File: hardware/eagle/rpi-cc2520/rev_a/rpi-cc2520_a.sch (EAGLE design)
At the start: 28 parts, among them P1 MOLEX_73251-135X, U1 CC2520, X1 NX2520SA

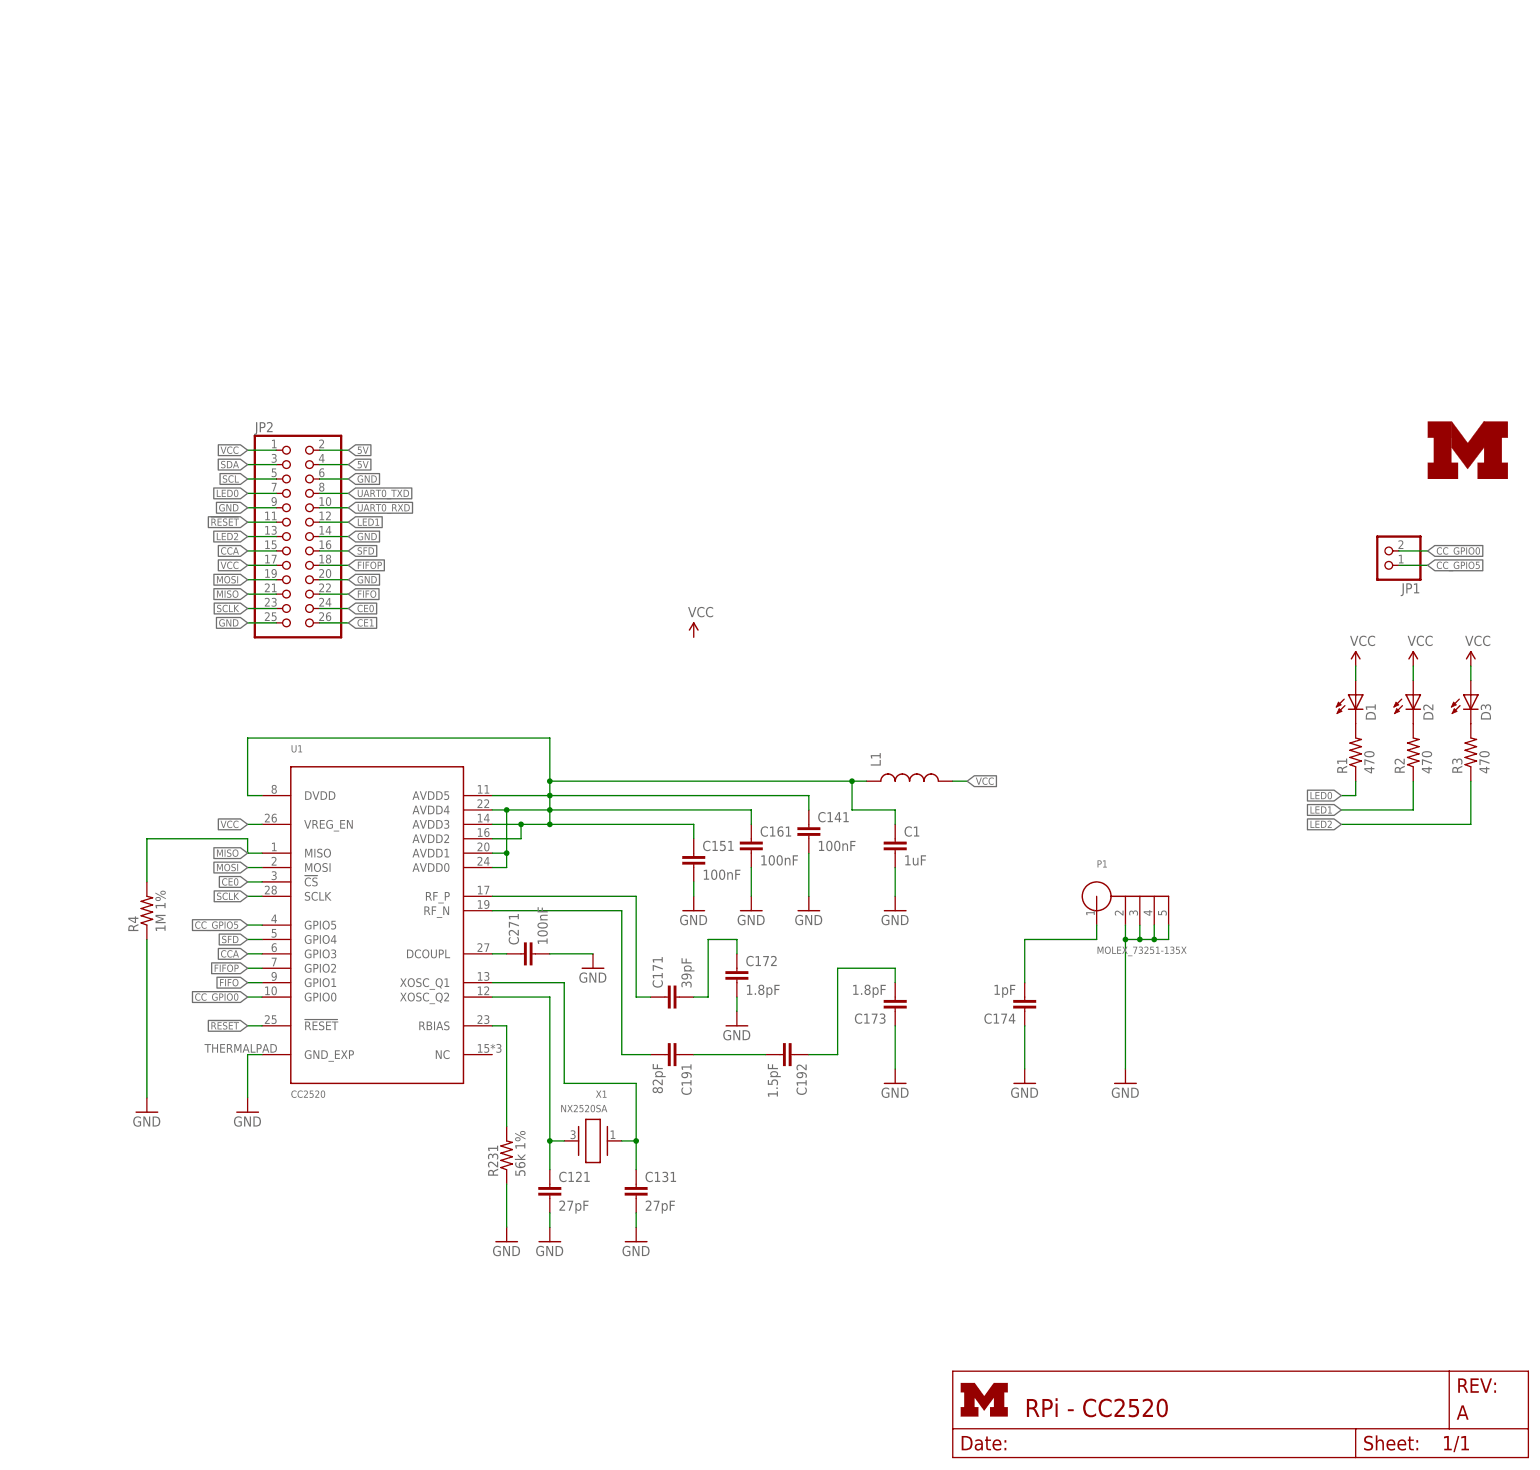
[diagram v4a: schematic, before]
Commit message: carefully laying out the sma antenna
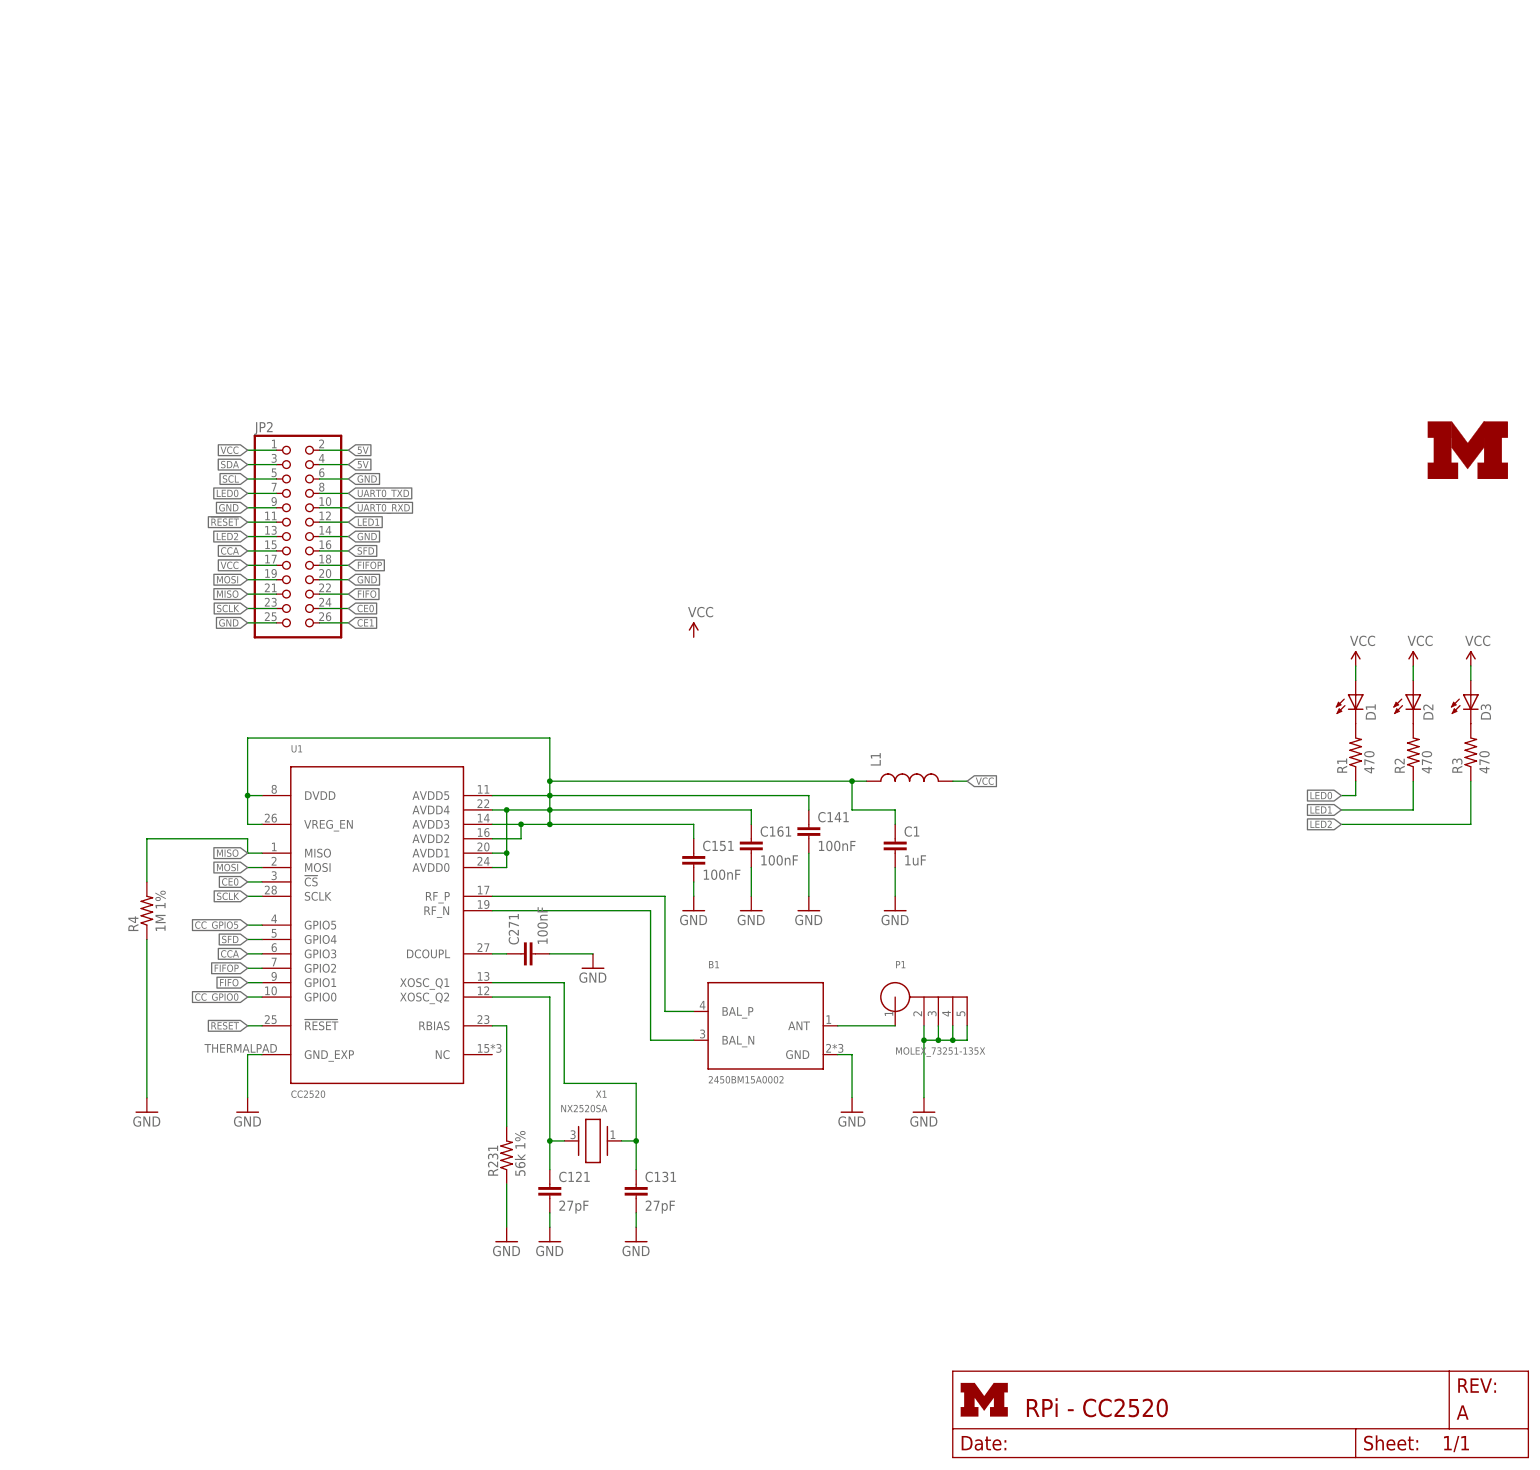
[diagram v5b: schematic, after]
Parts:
- removed C171: 39pF, rcl:C-EUC0402
- removed C172, C173: 1.8pF, rcl:C-EUC0402
- removed C174: 1pF, rcl:C-EUC0402
- removed C191: 82pF, rcl:C-EUC0402
- removed C192: 1.5pF, rcl:C-EUC0402
- removed JP1: (no value), pinhead:PINHD-1X2
- added B1: 2450BM15A0002, rpi-cc2520:2450BM15A0002
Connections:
- removed net N$10: C174.2, P1.P$1
- removed net N$4: C171.1, U1.RF_P
- removed net N$6: C191.2, U1.RF_N
- removed net N$8: C191.1, C192.2
- removed net N$9: C173.2, C192.1
- new net RF_N: B1.BAL_N, U1.RF_N
- new net RF_P: B1.BAL_P, U1.RF_P
- net CC_GPIO0: no longer JP1.2
- net CC_GPIO5: no longer JP1.1
- net GND: now also B1.GND; no longer C172.2, C173.1, C174.1
- net N$5: now also U1.VREG_EN
- net N$7: now also B1.ANT, P1.P$1; no longer C171.2, C172.1
- net VCC: no longer U1.VREG_EN
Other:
- moved on the sheet: P1

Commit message: added a ton of vias
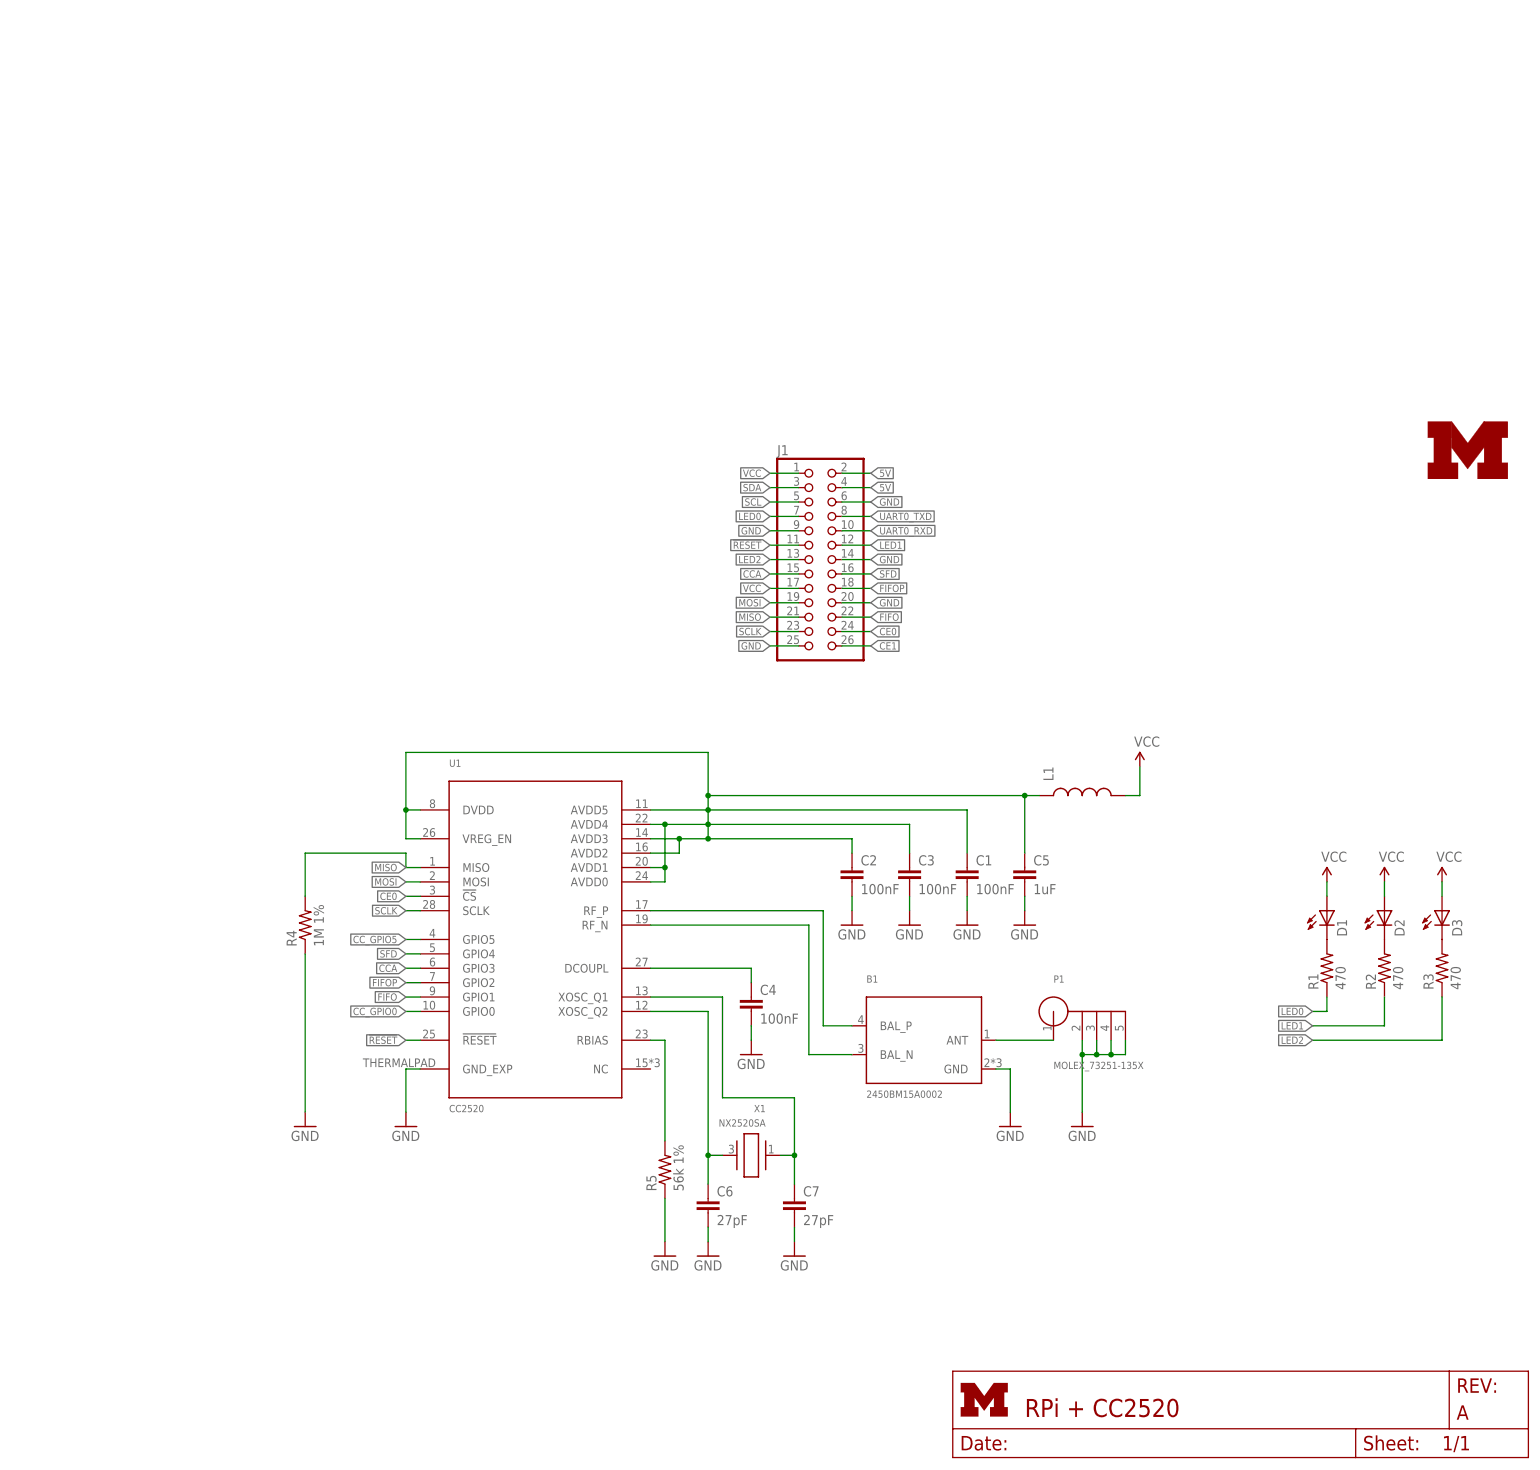
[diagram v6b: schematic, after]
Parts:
- removed C121, C131: 27pF, rcl:C-EUC0402
- removed C141, C151, C161, C271: 100nF, rcl:C-EUC0402
- removed JP2: (no value), pinhead:PINHD-2X13
- removed R231: 56k 1%, rcl:R-US_R0402
- added C2, C3, C4: 100nF, rcl:C-EUC0402
- added C5: 1uF, rcl:C-EUC0603
- added C6, C7: 27pF, rcl:C-EUC0402
- added J1: (no value), pinhead:PINHD-2X13
- added R5: 56k 1%, rcl:R-US_R0402
- C1: value 1uF -> 100nF; device rcl:C-EUC0603 -> rcl:C-EUC0402; DIGIKEY 490-1550-1-ND -> 490-1318-1-ND
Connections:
- net !RESET: now also J1.11; no longer JP2.11
- net 5V: now also J1.2, J1.4; no longer JP2.2, JP2.4
- net CCA: now also J1.15; no longer JP2.15
- net CE0: now also J1.24; no longer JP2.24
- net CE1: now also J1.26; no longer JP2.26
- net FIFO: now also J1.22; no longer JP2.22
- net FIFOP: now also J1.18; no longer JP2.18
- net GND: now also C2.2, C3.2, C4.2, C5.2, C6.2, C7.2, J1.14, J1.20, J1.25, J1.6, J1.9, R5.1; no longer C121.2, C131.2, C141.2, C151.2, C161.2, C271.2, JP2.14, JP2.20, JP2.25, JP2.6, JP2.9, R231.1
- net LED0: now also J1.7; no longer JP2.7
- net LED1: now also J1.12; no longer JP2.12
- net LED2: now also J1.13; no longer JP2.13
- net MISO: now also J1.21; no longer JP2.21
- net MOSI: now also J1.19; no longer JP2.19
- net N$11: now also C7.1; no longer C131.1
- net N$12: now also C4.1; no longer C271.1
- net N$13: now also C6.1; no longer C121.1
- net N$14: now also R5.2; no longer R231.2
- net N$5: now also C2.1, C3.1, C5.1; no longer C141.1, C151.1, C161.1
- net SCL: now also J1.5; no longer JP2.5
- net SCLK: now also J1.23; no longer JP2.23
- net SDA: now also J1.3; no longer JP2.3
- net SFD: now also J1.16; no longer JP2.16
- net UART0_RXD: now also J1.10; no longer JP2.10
- net UART0_TXD: now also J1.8; no longer JP2.8
- net VCC: now also J1.1, J1.17; no longer JP2.1, JP2.17
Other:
- moved on the sheet: B1, C1, D1, D2, D3, L1, P1, R1, R2, R3, R4, U1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
